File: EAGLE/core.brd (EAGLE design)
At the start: 20.3 x 35.6 mm, 47 parts, among them IC1 MCP1825S-3302E, Q1 MMDT3904, U2 STM32F10XCXT6, U3 SST25VF040B-S2, X1 USB-MICROB, X2 IPEX-20279-001E, Y1 32Khz, Y2 8Mhz

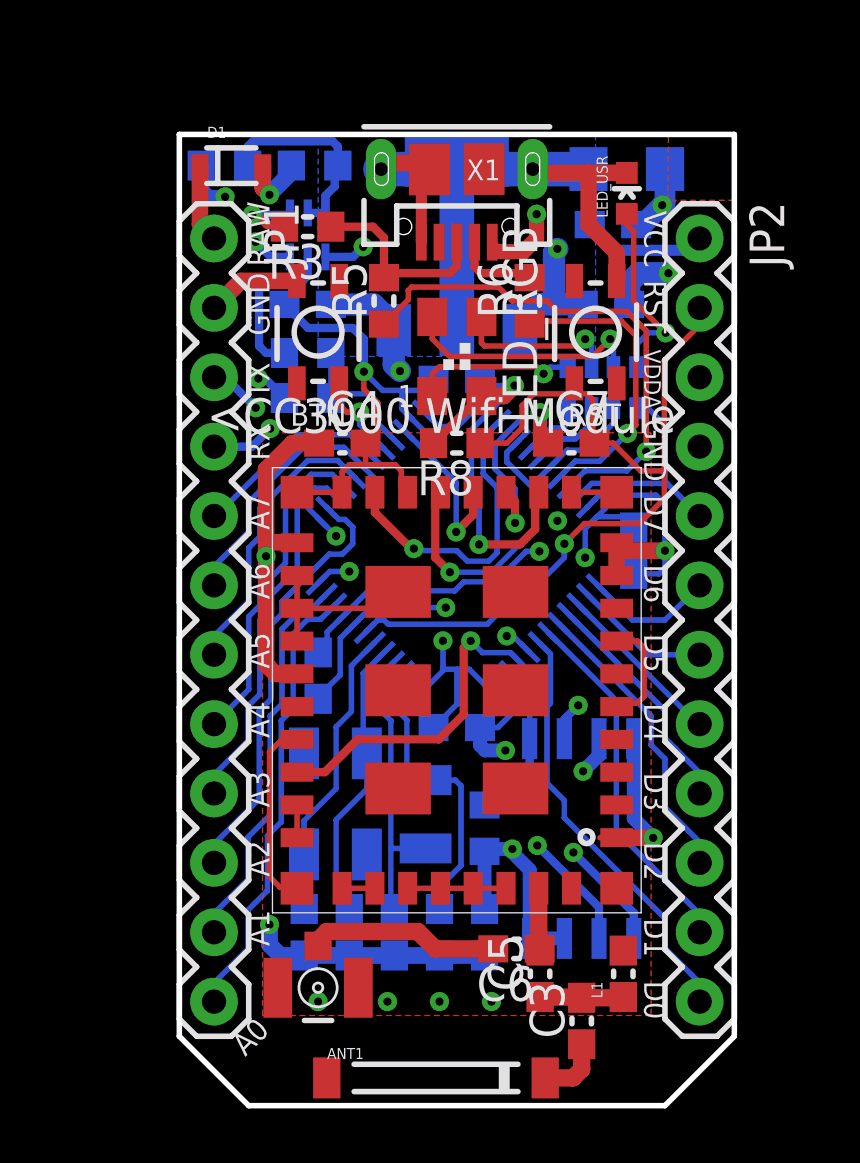
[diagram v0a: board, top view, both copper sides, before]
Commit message: added diode, maintained changed RGB LED footprint, moved the PCB
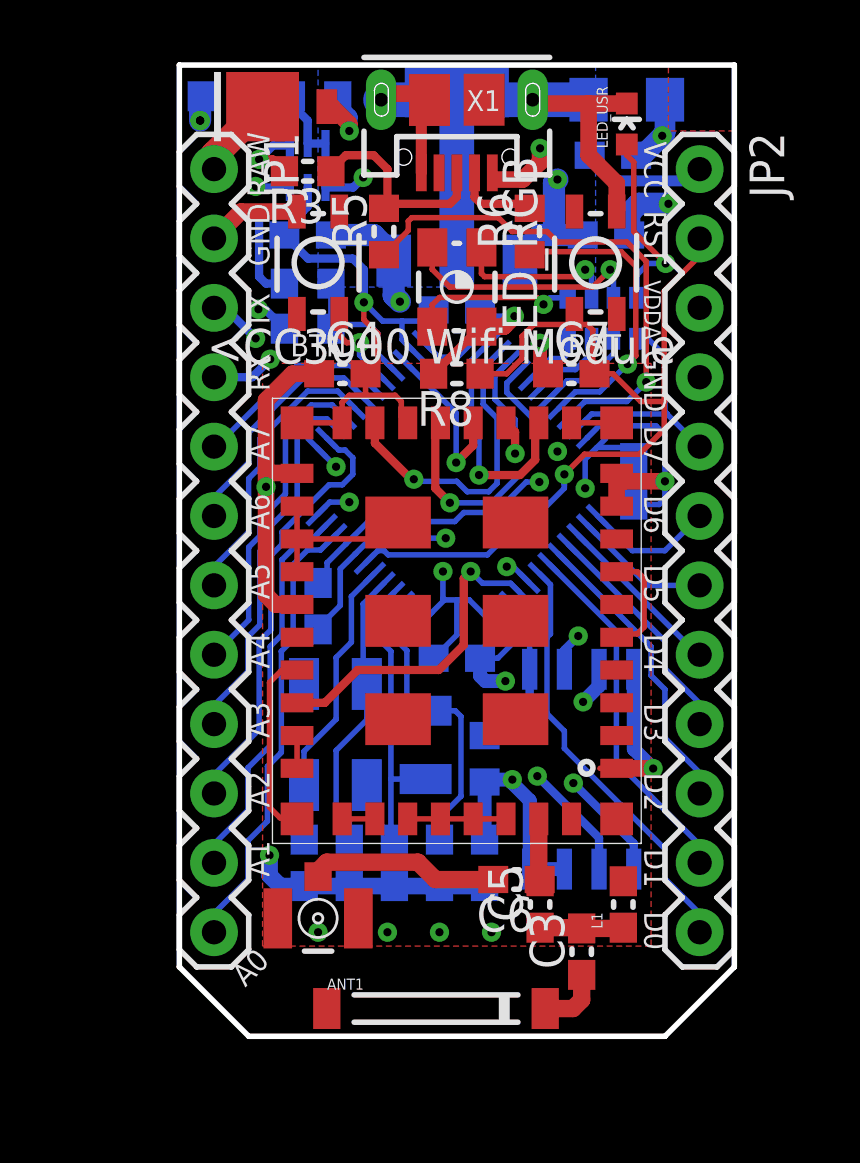
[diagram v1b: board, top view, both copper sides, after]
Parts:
- D1: value (none) -> DIODE; device SparkFun:SOD-323 -> Spark:DIODE-DO-220AA(SMP)
- moved BTN 2.54 mm to (5.08, 28.3)
- moved C13 2.54 mm to (10.2, 26.6)
- moved C4 2.54 mm to (5.97, 24.3)
- moved C7 2.54 mm to (14.4, 24.3)
- moved L2 2.54 mm to (15.9, 32.3)
- moved LED_USR 2.54 mm to (16.4, 33.4)
- moved R1 2.54 mm to (4.95, 34.4), turned to 180 degrees
- moved R2 2.54 mm to (1.65, 34.4)
- moved R4 2.54 mm to (4.70, 27.6)
- moved R7 2.54 mm to (4.70, 25.9)
- moved R8 2.54 mm to (10.2, 24.3)
- moved RESET 2.54 mm to (15.2, 28.3)
- moved RN1 2.54 mm to (15.5, 26.3)
- moved U$1 2.54 mm to (17.8, 33.0)
- moved U1 2.54 mm to (10.2, 15.2)
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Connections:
- net RAW: now also D1.CATHODE; no longer D1.1
- net UVCC: now also D1.ANODE; no longer D1.2
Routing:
- net N$13: track 7.42 -> 4.23 mm
- net UVCC: track 15.6 -> 12.7 mm
- net RAW: track 21.2 -> 22.2 mm
- net GND: track 112.6 -> 111.7 mm, vias 16 -> 17

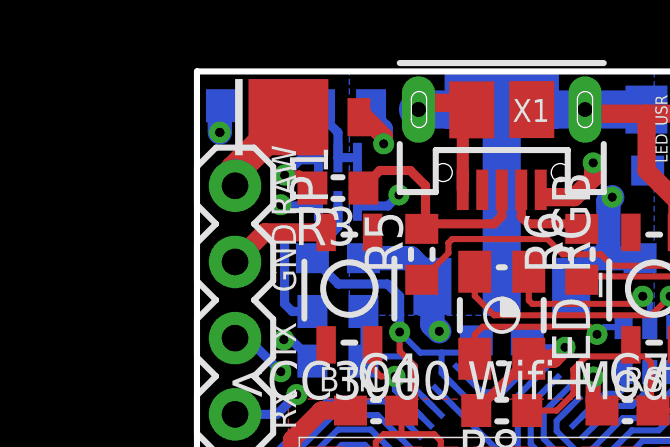
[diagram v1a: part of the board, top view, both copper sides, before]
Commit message: Via tweak to pass DRC
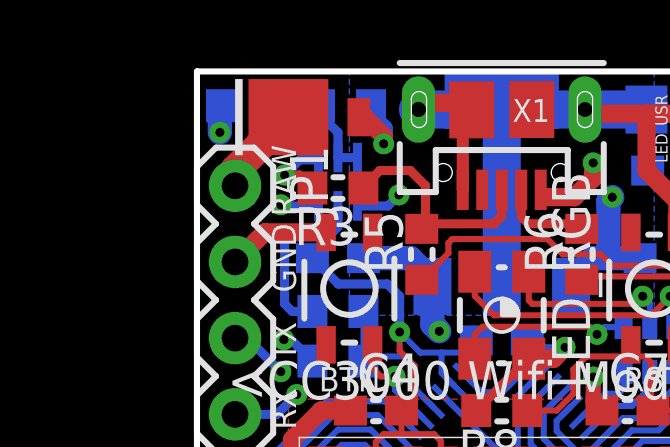
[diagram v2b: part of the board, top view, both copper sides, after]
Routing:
- net GND: vias 17 -> 16
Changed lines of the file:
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@@
 <?xml version="1.0" encoding="utf-8"?>
 <!DOCTYPE eagle SYSTEM "eagle.dtd">
-<eagle version="6.3">
+<eagle version="6.4">
 <drawing>
 <settings>
@@
 <setting verticaltext="up"/>
 </settings>
-<grid distance="0.1" unitdist="inch" unit="inch" style="lines" multiple="1" display="yes" altdistance="0.05" altunitdist="inch" altunit="inch"/>
+<grid distance="5" unitdist="mil" unit="mil" style="lines" multiple="1" display="yes" altdistance="0.05" altunitdist="inch" altunit="inch"/>
 <layers>
 <layer number="1" name="Top" color="4" fill="1" visible="yes" active="yes"/>
-<layer number="2" name="$GND" color="13" fill="1" visible="yes" active="yes"/>
+<layer number="2" name="$GND" color="13" fill="1" visible="no" active="yes"/>
 <layer number="3" name="Route3" color="4" fill="3" visible="no" active="no"/>
 <layer number="4" name="Route4" color="1" fill="4" visible="no" active="no"/>
@@
 <layer number="13" name="Route13" color="4" fill="5" visible="no" active="no"/>
 <layer number="14" name="Route14" color="1" fill="6" visible="no" active="no"/>
-<layer number="15" name="$+3V3" color="11" fill="1" visible="yes" active="yes"/>
+<layer number="15" name="$+3V3" color="11" fill="1" visible="no" active="yes"/>
 <layer number="16" name="Bottom" color="1" fill="1" visible="yes" active="yes"/>
 <layer number="17" name="Pads" color="2" fill="1" visible="yes" active="yes"/>
@@
 <wire x1="0.762" y1="34.3544" x2="0.762" y2="33.528" width="0.8128" layer="16"/>
 <via x="0.762" y="33.528" extent="1-16" drill="0.3"/>
-<via x="0.762" y="33.528" extent="1-16" drill="0.3"/>
 </signal>
 <signal name="RAW" class="1">
@@
 </signal>
 </signals>
+<errors>
+</errors>
 </board>
 </drawing>

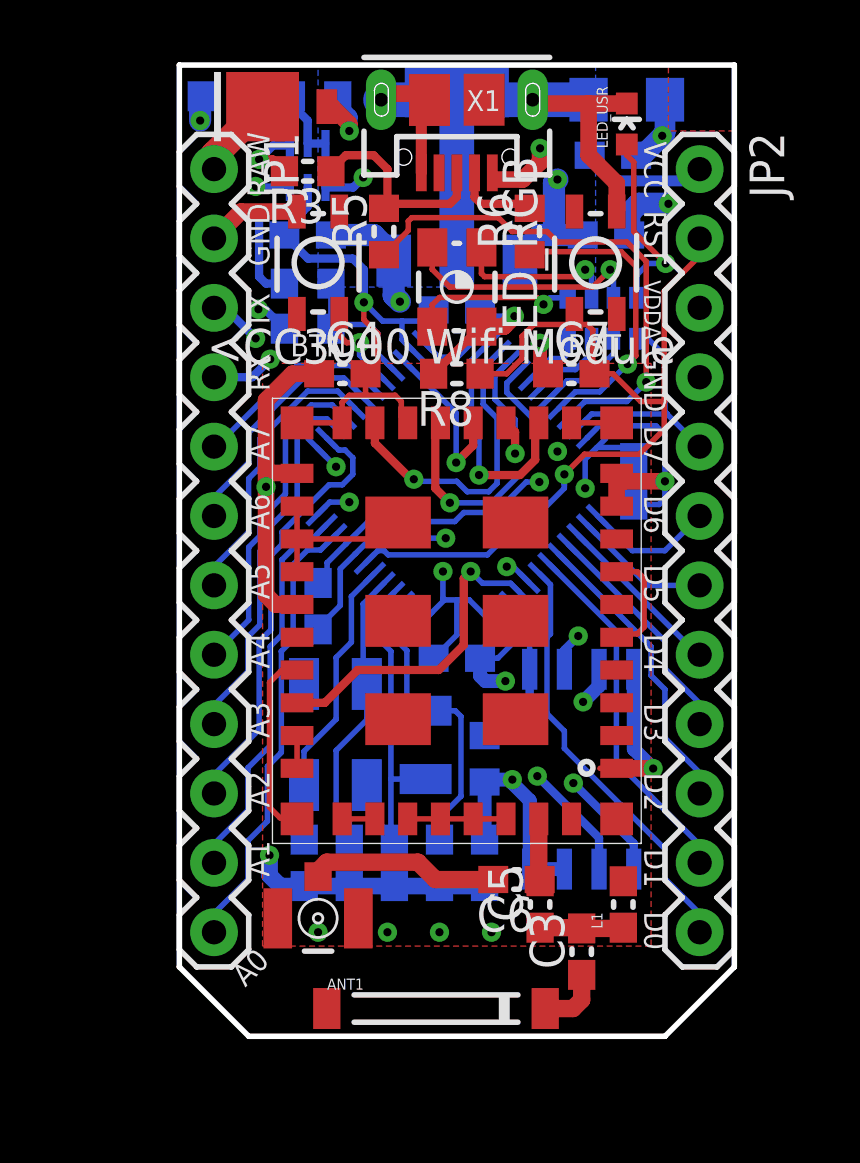
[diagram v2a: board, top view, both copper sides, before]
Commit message: Moved silkscreen on headers to bottom layer
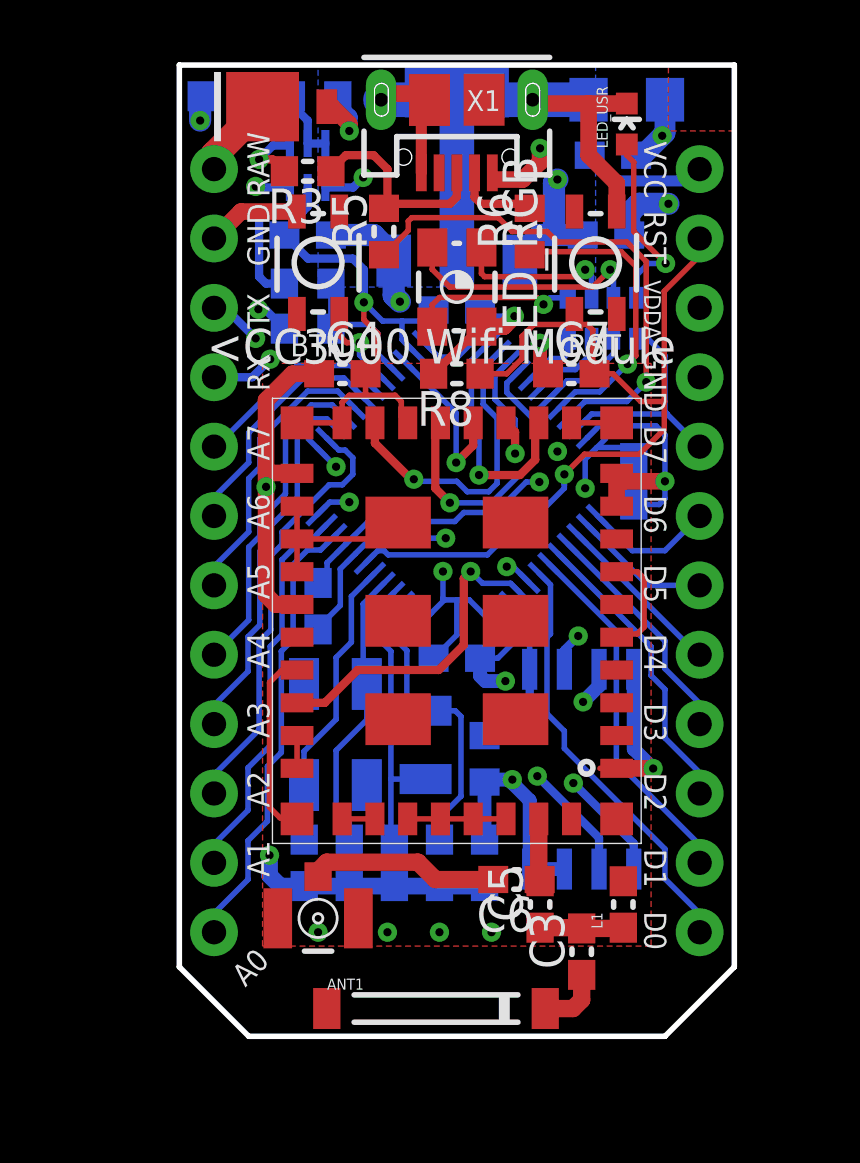
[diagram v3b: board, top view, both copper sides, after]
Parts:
- flipped JP1 to the bottom
- flipped JP2 to the bottom
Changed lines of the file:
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@@
 <attribute name="VALUE" x="15.648" y="33.339" size="0.4064" layer="28" rot="MR180"/>
 </element>
-<element name="JP1" library="Spark" package="1X12-SMALL-PADS" value="M12PTH" x="1.27" y="31.75" locked="yes" smashed="yes" rot="R270">
-<attribute name="NAME" x="3.0988" y="33.0962" size="1.27" layer="25" ratio="10" rot="R270"/>
+<element name="JP1" library="Spark" package="1X12-SMALL-PADS" value="M12PTH" x="1.27" y="31.75" smashed="yes" rot="MR270">
+<attribute name="NAME" x="-0.5588" y="33.0962" size="1.27" layer="26" ratio="10" rot="MR270"/>
 </element>
-<element name="JP2" library="Spark" package="1X12-SMALL-PADS" value="M12PTH" x="19.05" y="31.75" locked="yes" smashed="yes" rot="R270">
-<attribute name="NAME" x="20.8788" y="33.0962" size="1.27" layer="25" ratio="10" rot="R270"/>
+<element name="JP2" library="Spark" package="1X12-SMALL-PADS" value="M12PTH" x="19.05" y="31.75" smashed="yes" rot="MR270">
+<attribute name="NAME" x="17.2212" y="33.0962" size="1.27" layer="26" ratio="10" rot="MR270"/>
 </element>
 <element name="D1" library="Spark" package="DIODE-DO-220AA(SMP)" value="DIODE" x="3.048" y="34.036" locked="yes"/>

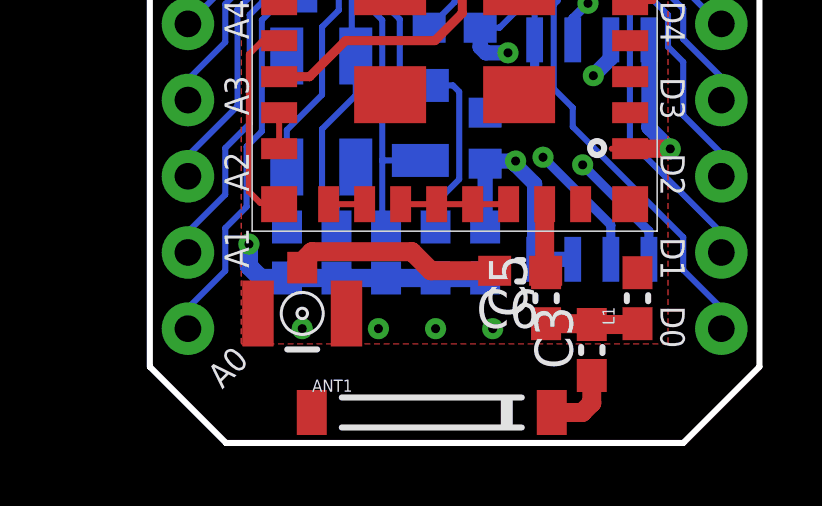
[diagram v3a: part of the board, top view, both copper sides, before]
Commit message: Created pi network
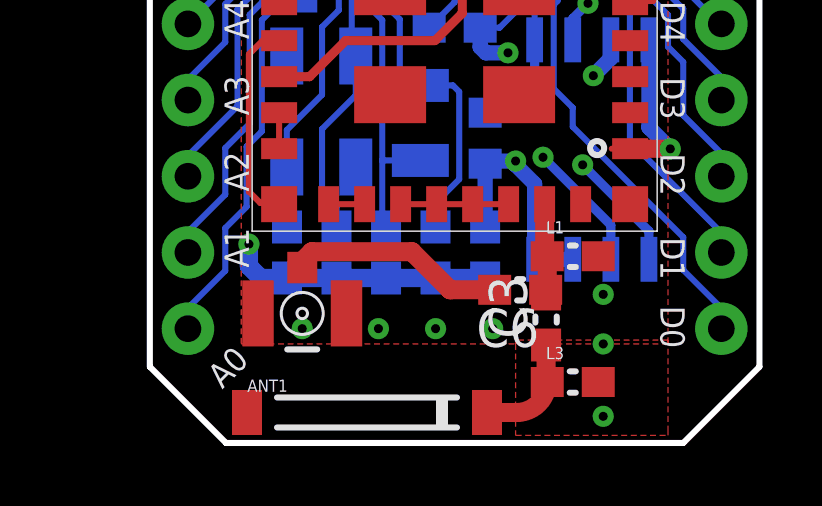
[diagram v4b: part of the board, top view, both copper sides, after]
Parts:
- removed C5: 10pF, rcl:C0603
- added L3: 2.2nH, SparkFun-Passives:0603
- moved L1 2.57 mm to (14.1, 6.22), turned to 0 degrees
- moved ANT1 2.16 mm to (7.24, 1.02)
- moved C3 1.83 mm to (13.2, 4.11)
- moved C6 0.63 mm to (12.3, 5.11)
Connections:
- removed net N$4: C5.2, C6.1, U1.RF_ANT
- net GND: now also L3.2
- net N$3: now also L3.1
- net N$5: now also C6.1, U1.RF_ANT; no longer C5.1
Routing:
- net N$4: track 2.31 -> 0.00 mm
- net N$3: track 2.38 -> 3.68 mm
- net GND: vias 16 -> 19
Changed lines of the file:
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@@
 </element>
 <element name="U1" library="CC3000" package="CC3000" value="" x="10.16" y="15.24" locked="yes" smashed="yes" rot="R180"/>
-<element name="L1" library="SparkFun-Passives" package="0603" value="2.2nH" x="16.256" y="4.826" locked="yes" smashed="yes" rot="R90">
-<attribute name="NAME" x="15.494" y="3.937" size="0.4064" layer="25" font="vector" rot="R90"/>
-<attribute name="VALUE" x="15.113" y="6.35" size="0.4064" layer="27" font="vector"/>
-</element>
-<element name="C3" library="rcl" package="C0603" value="2.2pF" x="14.732" y="3.0988" locked="yes" smashed="yes" rot="R90">
-<attribute name="NAME" x="14.097" y="2.4638" size="1.27" layer="25" rot="R90"/>
-<attribute name="VALUE" x="14.097" y="2.6162" size="0.4064" layer="27" rot="R180"/>
+<element name="L1" library="SparkFun-Passives" package="0603" value="2.2nH" x="14.097" y="6.223" smashed="yes">
+<attribute name="NAME" x="13.208" y="6.985" size="0.4064" layer="25" font="vector"/>
+<attribute name="VALUE" x="15.621" y="7.366" size="0.4064" layer="27" font="vector" rot="R270"/>
+</element>
+<element name="C3" library="rcl" package="C0603" value="2.2pF" x="13.208" y="4.1148" smashed="yes" rot="R90">
+<attribute name="NAME" x="12.573" y="3.4798" size="1.27" layer="25" rot="R90"/>
+<attribute name="VALUE" x="12.573" y="3.6322" size="0.4064" layer="27" rot="R180"/>
 </element>
 <element name="C4" library="rcl" package="C0603" value="100nF" x="5.969" y="24.257" locked="yes" smashed="yes">
@@
 </element>
 <element name="X2" library="Spark" package="IPEX-20279-001E" value="IPEX-20279-001E" x="5.08" y="4.318" locked="yes"/>
-<element name="C6" library="rcl" package="C0603" value="10pF" x="12.3444" y="5.7404" locked="yes" smashed="yes" rot="R180">
-<attribute name="NAME" x="12.9794" y="5.1054" size="1.27" layer="25" rot="R180"/>
-<attribute name="VALUE" x="10.6934" y="5.8674" size="0.4064" layer="27" rot="R180"/>
-</element>
-<element name="ANT1" library="Spark" package="AT8010" value="AT8010" x="9.398" y="1.016" locked="yes" smashed="yes">
-<attribute name="NAME" x="5.408" y="1.706" size="0.4064" layer="25"/>
-</element>
-<element name="C5" library="rcl" package="C0603" value="10pF" x="13.208" y="4.826" locked="yes" smashed="yes" rot="R90">
-<attribute name="NAME" x="12.573" y="4.191" size="1.27" layer="25" rot="R90"/>
-<attribute name="VALUE" x="12.573" y="4.064" size="0.4064" layer="27" rot="R180"/>
+<element name="C6" library="rcl" package="C0603" value="10pF" x="12.3444" y="5.1054" smashed="yes" rot="R180">
+<attribute name="NAME" x="12.9794" y="4.4704" size="1.27" layer="25" rot="R180"/>
+<attribute name="VALUE" x="10.6934" y="5.2324" size="0.4064" layer="27" rot="R180"/>
+</element>
+<element name="ANT1" library="Spark" package="AT8010" value="AT8010" x="7.239" y="1.016" smashed="yes">
+<attribute name="NAME" x="3.249" y="1.706" size="0.4064" layer="25"/>
 </element>
 <element name="C16" library="Spark" package="EIA3216" value="10uF" x="16.383" y="34.29" locked="yes" smashed="yes" rot="MR180">
@@
 </element>
 <element name="D1" library="Spark" package="DIODE-DO-220AA(SMP)" value="DIODE" x="3.048" y="34.036" locked="yes"/>
+<element name="L3" library="SparkFun-Passives" package="0603" value="2.2nH" x="14.097" y="2.032"/>
 </elements>
 <signals>
@@
 <wire x1="0.762" y1="34.3544" x2="0.762" y2="33.528" width="0.8128" layer="16"/>
 <via x="0.762" y="33.528" extent="1-16" drill="0.3"/>
+<contactref element="L3" pad="2"/>
+<polygon width="0.1524" layer="1" thermals="no">
+<vertex x="12.192" y="3.302"/>
+<vertex x="12.192" y="0.254"/>
+<vertex x="17.272" y="0.254"/>
+<vertex x="17.272" y="0.381"/>
+<vertex x="17.272" y="3.429"/>
+<vertex x="12.192" y="3.429"/>
+</polygon>
+<via x="15.113" y="0.889" extent="1-16" drill="0.3"/>
+<via x="15.113" y="3.302" extent="1-16" drill="0.3"/>
+<via x="15.113" y="4.953" extent="1-16" drill="0.3"/>
 </signal>
 <signal name="RAW" class="1">
@@
 <wire x1="16.383" y1="23.241" x2="17.0942" y2="23.9522" width="0.2032" layer="16"/>
 </signal>
-<signal name="N$4" class="2">
-<contactref element="U1" pad="RF_ANT"/>
-<contactref element="C6" pad="1"/>
-<contactref element="C5" pad="2"/>
-<wire x1="13.1944" y1="5.7404" x2="13.16" y2="5.7748" width="0.635" layer="1"/>
-<wire x1="13.16" y1="5.7748" x2="13.16" y2="7.96" width="0.635" layer="1"/>
-<wire x1="13.208" y1="5.7404" x2="13.208" y2="5.676" width="0.635" layer="1"/>
-<wire x1="13.208" y1="5.7404" x2="13.1944" y2="5.7404" width="0.4064" layer="1"/>
-</signal>
 <signal name="N$7">
 <contactref element="U1" pad="SCL_CC3000"/>
@@
 <contactref element="C6" pad="2"/>
 <contactref element="X2" pad="1"/>
-<wire x1="11.4944" y1="5.7404" x2="9.3726" y2="5.7404" width="0.635" layer="1"/>
-<wire x1="9.3726" y1="5.7404" x2="8.7376" y2="6.3754" width="0.635" layer="1"/>
 <wire x1="8.7376" y1="6.3754" x2="5.3975" y2="6.3754" width="0.635" layer="1"/>
 <wire x1="5.3975" y1="6.3754" x2="5.08" y2="6.0579" width="0.635" layer="1"/>
 <wire x1="5.08" y1="6.0579" x2="5.08" y2="5.8455" width="0.635" layer="1"/>
+<wire x1="8.7376" y1="6.3754" x2="10.0076" y2="5.1054" width="0.635" layer="1"/>
+<wire x1="10.0076" y1="5.1054" x2="11.4944" y2="5.1054" width="0.635" layer="1"/>
 </signal>
 <signal name="N$3" class="2">
 <contactref element="ANT1" pad="SIG"/>
 <contactref element="C3" pad="1"/>
-<wire x1="14.732" y1="2.2488" x2="14.732" y2="1.3335" width="0.635" layer="1"/>
-<wire x1="14.732" y1="1.3335" x2="14.4145" y2="1.016" width="0.635" layer="1"/>
-<wire x1="14.4145" y1="1.016" x2="13.398" y2="1.016" width="0.635" layer="1"/>
+<contactref element="L3" pad="1"/>
+<wire x1="13.208" y1="3.2648" x2="13.208" y2="2.071" width="0.635" layer="1"/>
+<wire x1="13.208" y1="2.071" x2="13.247" y2="2.032" width="0.635" layer="1"/>
+<wire x1="13.247" y1="2.032" x2="12.231" y2="1.016" width="0.635" layer="1" curve="-90"/>
+<wire x1="12.231" y1="1.016" x2="11.239" y2="1.016" width="0.635" layer="1"/>
 </signal>
 <signal name="N$5" class="2">
 <contactref element="C3" pad="2"/>
 <contactref element="L1" pad="1"/>
-<contactref element="C5" pad="1"/>
-<wire x1="13.208" y1="3.976" x2="14.7048" y2="3.976" width="0.635" layer="1"/>
-<wire x1="14.7048" y1="3.976" x2="14.732" y2="3.9488" width="0.635" layer="1"/>
-<wire x1="14.732" y1="3.9488" x2="16.2288" y2="3.9488" width="0.635" layer="1"/>
-<wire x1="16.2288" y1="3.9488" x2="16.256" y2="3.976" width="0.635" layer="1"/>
+<contactref element="U1" pad="RF_ANT"/>
+<contactref element="C6" pad="1"/>
+<wire x1="13.16" y1="7.96" x2="13.16" y2="6.31" width="0.635" layer="1"/>
+<wire x1="13.16" y1="6.31" x2="13.247" y2="6.223" width="0.635" layer="1"/>
+<wire x1="13.247" y1="6.223" x2="13.247" y2="5.158" width="0.635" layer="1"/>
+<wire x1="13.247" y1="5.158" x2="13.1944" y2="5.1054" width="0.635" layer="1"/>
+<wire x1="13.208" y1="4.9648" x2="13.1944" y2="5.1054" width="0" layer="19" extent="1-1"/>
 </signal>
 <signal name="LED1">
